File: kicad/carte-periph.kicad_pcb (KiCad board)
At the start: 2 copper layers, 80 x 72.4 mm, 28 parts, among them J1 PDB, J2 PWR_IN, J3 PROG, J8 I2C, J9 I2C, U1 Conn_periph, U2 PIC24FJ128GA104, Y1 10MHz

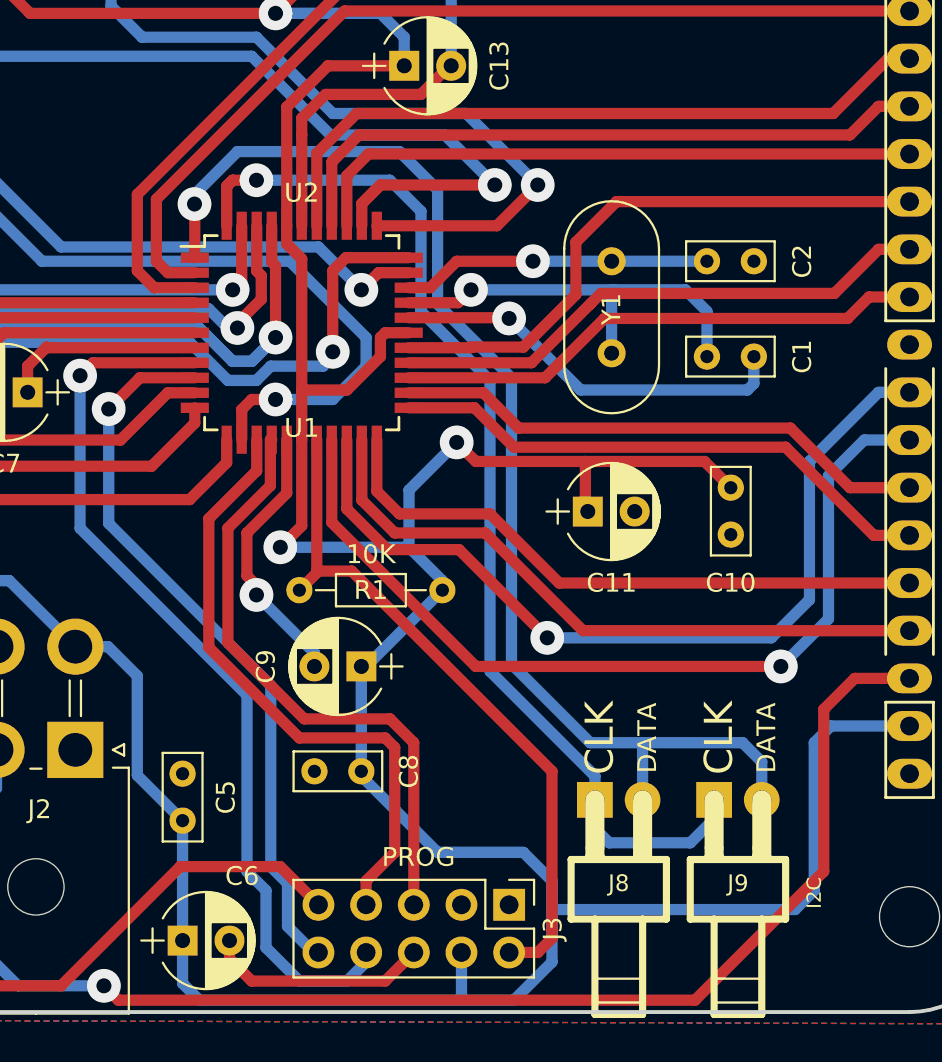
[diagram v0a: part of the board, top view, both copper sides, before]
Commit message: Retouche des connecteurs I2C et ajout du 5V sur le connecteur de programmation
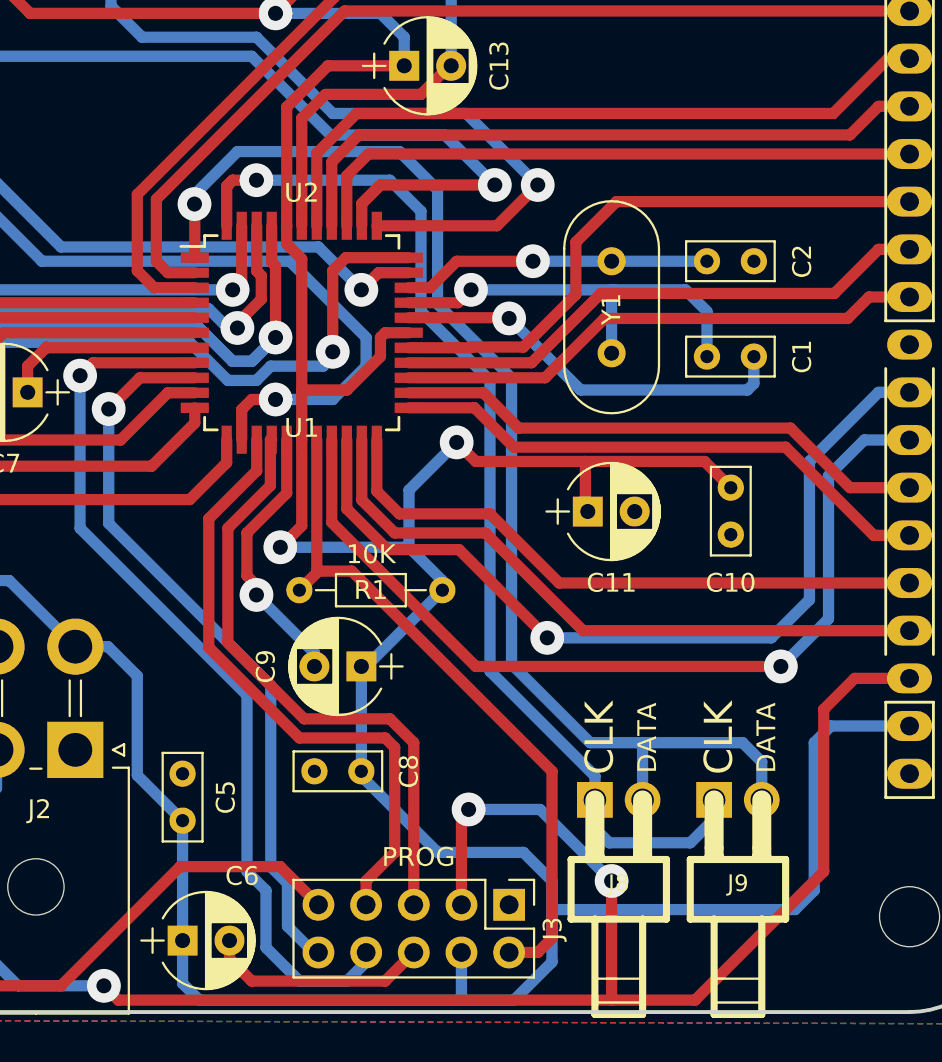
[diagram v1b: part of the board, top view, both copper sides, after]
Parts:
- J8, J9: footprint Epsa:KK_2C -> EPSA_KK2C:KK_2C
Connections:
- J3 pad 3: (no net) -> +5V
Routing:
- net +5V: track 157.9 -> 178.7 mm, vias 1 -> 3

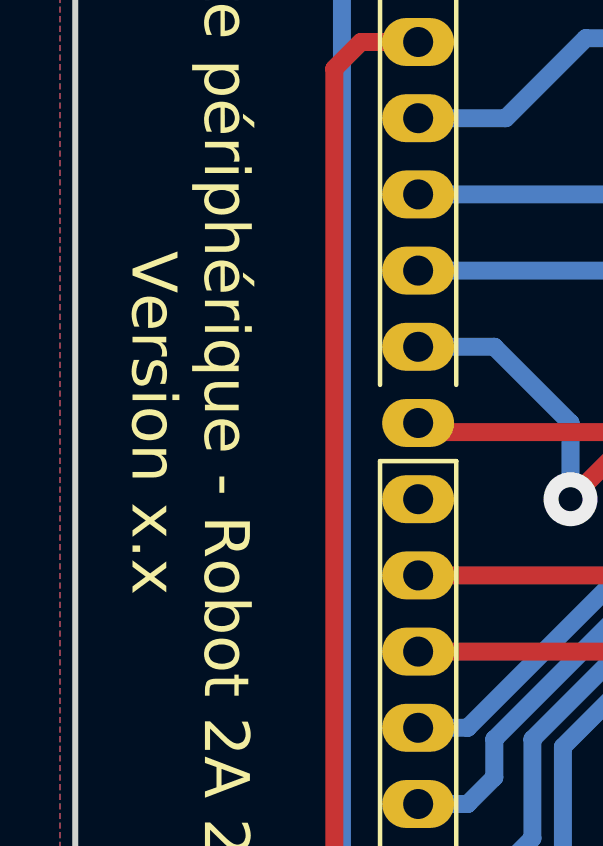
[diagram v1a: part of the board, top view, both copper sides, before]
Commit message: Mise à jour des cartouches en vue de la release
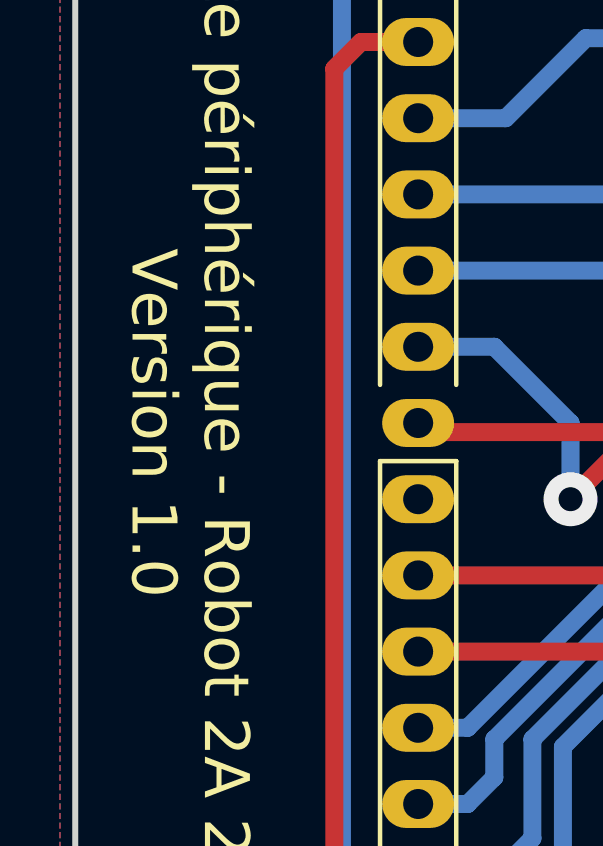
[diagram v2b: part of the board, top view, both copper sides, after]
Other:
- board text added: "Carte périphérique - Robot 2A 2018 Version 1.0"
- board text removed: "Carte périphérique - Robot 2A 2018 Version x.x"
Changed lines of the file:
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@@
     (links 97)
     (no_connects 0)
-    (area 35.459999 23.394999 115.670001 95.985001)
+    (area 35.052 22.86 116.332001 96.584001)
     (thickness 1.6)
     (drawings 13)
@@
   (title_block
     (title "Carte standard périphériques - Robot 2A année 2018")
-    (rev vx.x)
+    (date 2018-04-22)
+    (rev v1.0)
     (company "Centrale Lyon")
     (comment 1 "Contcter G. CHARREAUX (chxguillaume@gmail.com)")
@@
   (gr_arc (start 40.64 28.575) (end 35.56 28.575) (angle 90) (layer Edge.Cuts) (width 0.2))
   (gr_arc (start 110.49 28.575) (end 110.49 23.495) (angle 90) (layer Edge.Cuts) (width 0.2))
-  (gr_text "Carte périphérique - Robot 2A 2018\nVersion x.x" (at 39.37 57.785 270) (layer F.SilkS)
+  (gr_text "Carte périphérique - Robot 2A 2018\nVersion 1.0" (at 39.37 57.785 270) (layer F.SilkS)
     (effects (font (size 1.5 1.5) (thickness 0.3)))
   )
